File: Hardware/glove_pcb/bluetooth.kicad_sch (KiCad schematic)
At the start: 13 parts, among them U16 BM70BLES1FC2-0B04AA, U17 MCP111T-195I/TT, U18 74LVC1T45GW_125, U19 74LVC1T45GW_125

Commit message: Assign footprints and import all parts into pcb editor
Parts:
- JP1: footprint (none) -> Connector_PinHeader_2.54mm:PinHeader_1x02_P2.54mm_Vertical
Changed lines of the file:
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@@
       (effects (font (size 1.27 1.27)) (justify left))
     )
-    (property "Footprint" "" (at 116.84 74.93 0)
+    (property "Footprint" "Connector_PinHeader_2.54mm:PinHeader_1x02_P2.54mm_Vertical" (at 116.84 74.93 0)
       (effects (font (size 1.27 1.27)) hide)
     )

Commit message: Reworking placing
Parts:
- U16: footprint Glove_Footprints:BM70BLES1FC2_MCH -> Glove_Footprints:BM70BLES1FC2_MCH(2)

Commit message: More intermediate changes
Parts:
- renumbered C52 to C53, C53 to C54, C54 to C55, C55 to C56

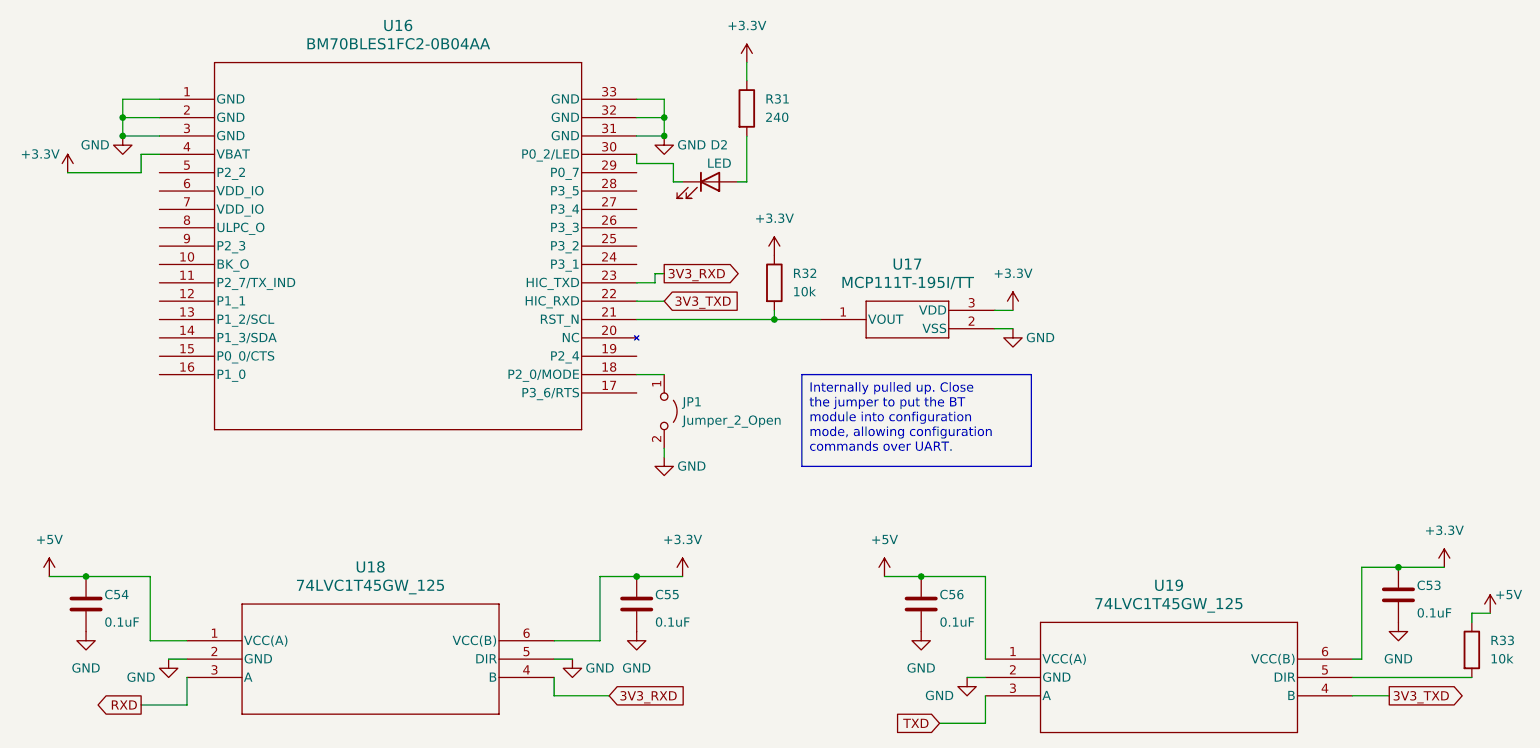
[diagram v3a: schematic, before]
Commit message: More improvements and routing fixes
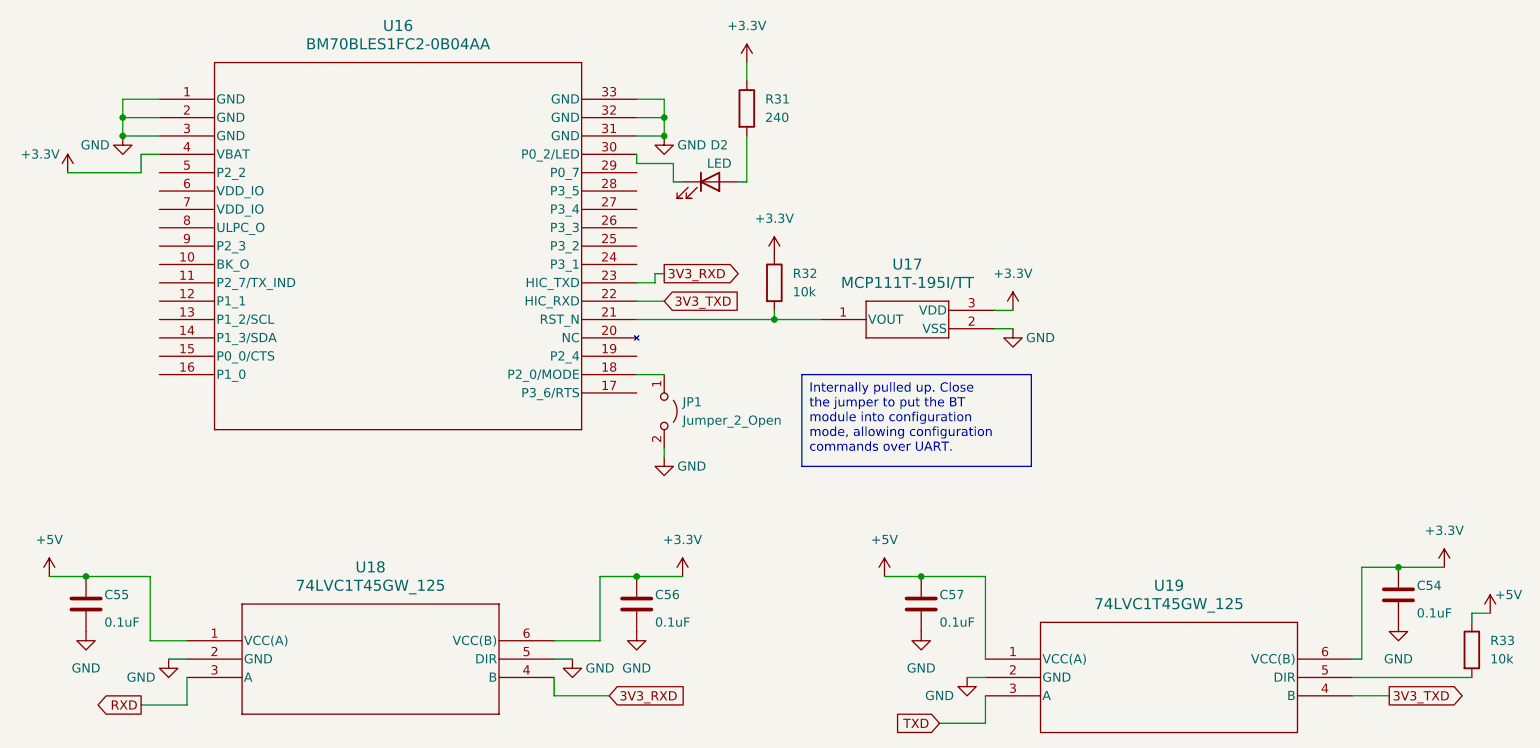
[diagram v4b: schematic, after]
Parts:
- renumbered C53 to C54, C54 to C55, C55 to C56, C56 to C57
